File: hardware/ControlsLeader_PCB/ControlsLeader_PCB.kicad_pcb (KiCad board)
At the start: 2 copper layers, 135 x 72 mm, 204 parts, among them IC1 TCAN337DCNR, IC2 AP2205-W5-7, J1 CarCANConnector_Out, J11 EStop1, J12 SteeringAngleConn_01x04, J13 Supp_Out, J14 SteeringConn_01x06, J15 IgnConn_01x04, J16 Conn_01x03, J17 Conn_01x02, J2 PeripheralCAN_out, J3 CarCANConnector_In, J4 PeripheralCAN_in, J6 Conn_2Rows-13Pins, J7 Conn_01x04, J8 Dash_Lsom_Horn_Lights_PWR, J9 Supp_In, Q1 NMOS, Q10 NMOS, Q11 NMOS, Q12 NMOS, Q13 NMOS, Q14 NMOS, Q15 NMOS, Q16 NMOS, Q17 NVMFWS1D7N04XMT1G, Q18 NMOS, Q2 NVMFWS1D7N04XMT1G, Q3 NMOS, Q4 NMOS, Q5 NMOS, Q6 NVMFWS1D7N04XMT1G, Q7 NMOS, Q8 NMOS, Q9 NMOS, U1 CDSOT23-T24CAN, U2 LeaderSOM, U6 TPS5405DR

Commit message: Final fixes
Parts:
- F4: value 0603L025YR -> 0805L100WR; footprint 0603L025YR:FUSC1608X75N -> 0805L100WR:FUSC2114X180N
- moved CC_Term2 64.1 mm to (116.1, 123.1), turned to 0 degrees
- moved F4 0.08 mm to (192.1, 73.9)
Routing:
- net /FDCAN2_RX: track 53.4 -> 78.5 mm, vias 2 -> 4
- net /FDCAN2_TX: track 60.2 -> 81.9 mm
- net GND: vias 198 -> 196
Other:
- board text added: "10A"
- board text added: "5A"
- board text added: "Validated"

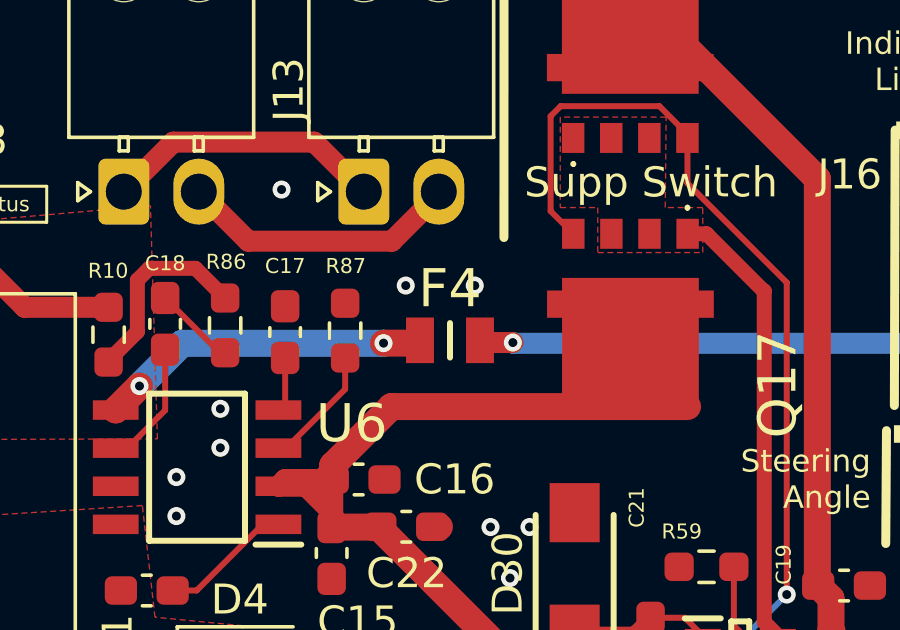
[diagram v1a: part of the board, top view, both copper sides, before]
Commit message: updated jlc parts list
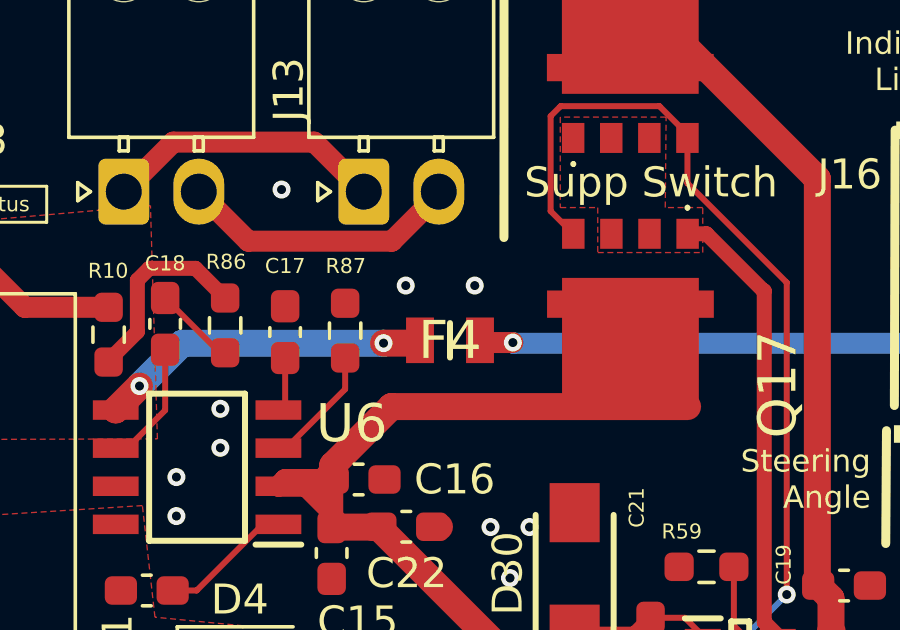
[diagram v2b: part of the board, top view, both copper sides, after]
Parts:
- C1, C10, C11, C12, C13, C14, C2, C28, C3, C4, C5, C6, C7, C8, C9: value 5uF -> 2.2uF
